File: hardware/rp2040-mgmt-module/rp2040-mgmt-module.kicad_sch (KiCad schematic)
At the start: 38 parts, among them J1 Bus_PCI_Express_x1, J2 USB_B_Micro, J3 RJ45_Hanrun_HR911105A_Horizon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, J4 Conn_01x03_Socket, Q1 2N7002KQ-7, SW1 SW_Push, U1 AMS1117-3.3, U2 W25Q32JVSSIQ, U3 RP2040, U4 W5500, Y1 X322512MSB4SI, Y2 X322512MSB4SI

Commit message: feat: initial rp2040 mgmt module layout finished
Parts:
- removed D1: BAT60B, Diode_SMD:D_SOD-323, symbol Diode:BAT60A
- removed Q1: 2N7002KQ-7, Package_TO_SOT_SMD:SOT-23, symbol Transistor_FET:2N7002
- added C1, C6: 1uF, Capacitor_SMD:C_0402_1005Metric, symbol Device:C
- added C10, C12, C13, C14, C17, C3, C5, C7, C8, C9: 100nF, Capacitor_SMD:C_0402_1005Metric, symbol Device:C
- added C11: 4.7uF, Capacitor_SMD:C_0402_1005Metric, symbol Device:C
- added C15: 22nF, Capacitor_SMD:C_0402_1005Metric, symbol Device:C
- added C16, C18: 6.8nF, Capacitor_SMD:C_0402_1005Metric, symbol Device:C
- added C2, C4: 39pF, Capacitor_SMD:C_0402_1005Metric, symbol Device:C
- added C36: 10uF, Capacitor_SMD:C_0402_1005Metric, symbol Device:C
- added D2: RED, LED_SMD:LED_0603_1608Metric, symbol Device:LED
- added D3: GREEN, LED_SMD:LED_0603_1608Metric, symbol Device:LED
- added D4: Neopixel Side Light SK6812, Local Library:LED_Neopixel_Side_Light_SK6812, symbol usb-pd-psu:LED_Neopixel_Side_Light_SK6812
- added J5: ADC, Connector_PinSocket_2.54mm:PinSocket_1x02_P2.54mm_Vertical, symbol Connector:Conn_01x02_Pin
- added J6: UART, Connector_PinHeader_2.54mm:PinHeader_1x04_P2.54mm_Vertical, symbol Connector:Conn_01x04_Pin
- added J7: UART, Connector_PinHeader_2.54mm:PinHeader_1x06_P2.54mm_Vertical, symbol Connector:Conn_01x06_Pin
- added R1, R3, R5: 4.7K, Resistor_SMD:R_0402_1005Metric, symbol Device:R
- added R10, R12, R13, R14: 49.9R, Resistor_SMD:R_0402_1005Metric, symbol Device:R
- added R11: 12.4K 1%, Resistor_SMD:R_0402_1005Metric, symbol Device:R
- added R15: 10R 1%, Resistor_SMD:R_0402_1005Metric, symbol Device:R
- added R18, R19, R20, R21: 470R, Resistor_SMD:R_0402_1005Metric, symbol Device:R
- added R2, R22: 1K, Resistor_SMD:R_0402_1005Metric, symbol Device:R
- added R23: 200R, Resistor_SMD:R_0402_1005Metric, symbol Device:R
- added R24: 1R, Resistor_SMD:R_0402_1005Metric, symbol Device:R
- added R4: 1M, Resistor_SMD:R_0402_1005Metric, symbol Device:R
- added R6, R7, R8, R9: 3.3R, Resistor_SMD:R_0402_1005Metric, symbol Device:R
- added SW2: RESET, Local Library:XKB_TS-1101_SWITCH, symbol Switch:SW_Push
- C19: renamed from C3; footprint Capacitor_SMD:C_0805_2012Metric -> Capacitor_SMD:C_0402_1005Metric; LCSC (none) -> C15525
- C20: renamed from C4; footprint Capacitor_SMD:C_0805_2012Metric -> Capacitor_SMD:C_0402_1005Metric; LCSC (none) -> C15525
- C21: renamed from C5; LCSC (none) -> C1525
- C22: renamed from C6; LCSC (none) -> C1525
- C23: renamed from C7; LCSC (none) -> C1525
- C24: renamed from C8; LCSC (none) -> C52923
- C25: renamed from C9; LCSC (none) -> C1525
- C26: renamed from C10; LCSC (none) -> C52923
- C27: renamed from C11; LCSC (none) -> C1525
- C30: renamed from C12; LCSC (none) -> C1525
- C31: renamed from C13; LCSC (none) -> C1525
- C32: renamed from C14; LCSC (none) -> C1525
- C33: renamed from C15; LCSC (none) -> C1525
- C34: renamed from C16; footprint Capacitor_SMD:C_0805_2012Metric -> Capacitor_SMD:C_0402_1005Metric; LCSC (none) -> C15525
- C35: renamed from C17; LCSC (none) -> C1525
- J1: renamed from J4; value Conn_01x03_Socket -> SWD; symbol Connector:Conn_01x03_Socket -> Connector:Conn_01x03_Pin; now in the parts list
- J2: renamed from J1; now not fitted
- J3: renamed from J2; footprint Connector_USB:USB_Micro-B_Amphenol_10103594-0001LF_Horizontal -> Connector_USB:USB_Micro-B_XKB_U254-051T-4BH83-F1S; JLCPCB_CORRECTION (none) -> 0;-1.1;0; LCSC (none) -> C319160
- J4: renamed from J3; value RJ45_Hanrun_HR911105A_Horizontal -> RJ45_Hanrun_HR913550A_Horizontal; JLCPCB_CORRECTION (none) -> 4.4;4.4;180
- R16: renamed from R1; LCSC (none) -> C11702
- R17: renamed from R2; now not fitted; now left out of the parts list
- R25: renamed from R4; LCSC (none) -> C25100
- R26: renamed from R5; LCSC (none) -> C25100
- R29: renamed from R3; LCSC (none) -> C11702
- SW1: value SW_Push -> BOOT
- U1: renamed from U4; JLCPCB_CORRECTION (none) -> 0;0;-90
- U2: renamed from U1; JLCPCB_CORRECTION (none) -> 0;0;180
- U3: renamed from U2; JLCPCB_CORRECTION (none) -> 0;0;-90
- Y1: renamed from Y2; value X322512MSB4SI -> X322525MRB4SI
- renumbered C1 to C28, C2 to C29, R6 to R27, R7 to R28, U3 to U4, Y1 to Y2
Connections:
- net ENABLE is gone; now on net I2C_A1: U4.36 (GPIO24)
- net GPIO0 is gone; now on net UART_TX: U4.2 (GPIO0)
- net GPIO22 is gone; now on net I2C_A0: U4.34 (GPIO22)
- net GPIO29_ADC3 is gone; now on net OVERLOAD: U4.41 (GPIO29_ADC3)
- net GPIO6 is gone; now on net LED_DIN: U4.8 (GPIO6)
- net +5V: now also D4.2 (VDD)
- net ALERT: now also J2.B11 (~{WAKE})
- net GND: now also J4.8, J4.SH, U1.14 (AGND), U1.16 (AGND), U1.19 (AGND), U1.29 (GND), U1.3 (AGND), U1.48 (AGND), U1.9 (AGND), Y1.2, Y1.4, C1.2, C10.2, C11.2, C12.2, C13.2, C14.2, C15.1, C17.2, C2.2, C3.2, C36.2, C4.2, C5.2, C6.2, C7.2, C8.2, C9.2, D2.1 (K), D3.1 (K), D4.4 (GND), J6.1 (Pin_1), J7.1 (Pin_1), R11.1, R24.1, SW2.1
- net GPIO10: now also J7.5 (Pin_5)
- net GPIO11: now also J7.6 (Pin_6)
- net GPIO16: now also U1.34 (MISO)
- net GPIO17: now also U1.32 (~{SCS}), R5.2
- net GPIO18: now also U1.33 (SCLK)
- net GPIO19: now also U1.35 (MOSI)
- net GPIO20: now also U1.37 (~{RST}), R1.1
- net GPIO21: now also U1.36 (~{INT}), R3.2
- net GPIO25: now also R21.1
- net GPIO27_ADC1: now also J5.1 (Pin_1)
- net GPIO8: now also J7.3 (Pin_3)
- net GPIO9: now also J7.4 (Pin_4)
- net I2C_A2: now also U4.35 (GPIO23)
- net LED_DIN: now also D4.1 (DIN); no longer U4.3 (GPIO1)
- net OVERLOAD: no longer U4.35 (GPIO23)
- net RUN: now also R22.2
- net at U1.1 (TXN): now also R6.1
- net at U1.10 (EXRES1): now also R11.2
- net +3.3VA: now reaches U1.11 (AVDD), U1.15 (AVDD), U1.17 (AVDD), U1.21 (AVDD), U1.4 (AVDD), U1.8 (AVDD)
- net +3.3VA: now also FB1.2, C10.1, C12.1, C14.1, C17.1, C6.1, C7.1, C8.1, R10.1, R12.1, R15.1
- net at U1.2 (TXP): now also R7.2
- net at U1.20 (TOCAP): now also C11.1
- net at U1.22 (1V2O): now also C9.1
- net LINK_LED: now reaches U1.25 (LINKLED)
- net LINK_LED: now also R20.2
- net ACT_LED: now reaches U1.27 (ACTLED)
- net ACT_LED: now also R19.2
- net +3.3V: now reaches U1.28 (VDD)
- net +3.3V: now also C20.1, C21.1, C25.1, C26.1, C27.1, C30.1, C31.1, C32.1, C33.1, C34.1, C35.1, FB1.1, J2.B10 (3.3Vaux), J4.12, J4.9, R17.1, U1.43 (PMODE2), U1.44 (PMODE1), U1.45 (PMODE0), U2.2 (VO), U3.8 (VCC), U4.1 (IOVDD), U4.10 (IOVDD), U4.22 (IOVDD), U4.33 (IOVDD), U4.42 (IOVDD), U4.44 (VREG_IN), U4.48 (USB_VDD), U4.49 (IOVDD), C1.1, C3.1, C36.1, C5.1, J6.2 (Pin_2), J7.2 (Pin_2), R1.2, R18.1, R23.1, R3.1, R5.1
- net at U1.30 (XI/CLKIN): now also Y1.1, C2.1, R4.1
- net at U1.31 (XO): now also R2.1, R4.2
- net at U1.5 (RXN): now also R9.1
- net at U1.6 (RXP): now also R8.2
- net at Y1.3: now also C4.1, R2.2
- net TX_D+: now reaches J4.1 (TD+)
- net TX_D+: now also R12.2, R7.1
- net at J4.10: now also R20.1
- net at J4.11: now also R19.1
- net TX_D-: now reaches J4.2 (TD-)
- net TX_D-: now also R10.2, R6.2
- net RX_D+: now reaches J4.3 (RD+)
- net RX_D+: now also C16.2
- net at J4.4 (TCT): now also C15.2, R15.2
- net at J4.5 (RCT): now also C13.1, R13.1, R14.1
- net RX_D-: now reaches J4.6 (RD-)
- net RX_D-: now also C18.2
- net UART_TX: now reaches J2.A13 (REFCLK+)
- net UART_TX: now also J6.3 (Pin_3)
- net UART_RX: now reaches J2.A14 (REFCLK-)
- net UART_RX: now also U4.3 (GPIO1), J6.4 (Pin_4)
- removed net +3V3: C20.1, C21.1, C25.1, C26.1, C27.1, C30.1, C31.1, C32.1, C33.1, C34.1, C35.1, J2.B10 (3.3Vaux), R17.1, U2.2 (VO), U3.8 (VCC), U4.1 (IOVDD), U4.10 (IOVDD), U4.22 (IOVDD), U4.33 (IOVDD), U4.42 (IOVDD), U4.43 (ADC_AVDD), U4.44 (VREG_IN), U4.48 (USB_VDD), U4.49 (IOVDD)
- net IMON renamed GPIO28_ADC2
- net GPIO28_ADC2: now also J5.2 (Pin_2)
- net ~{USB_BOOT}: no longer names the net of R16.2, SW1.2
- new net: R22.1, SW2.2
- new net: D2.2 (A), R18.2
- new net: C16.1, R14.2, R8.1
- new net: C18.1, R13.2, R9.2
- new net: D3.2 (A), R21.2
- new net ADC_AVDD: R23.2, R24.2, U4.43 (ADC_AVDD)
- no-connect marks 12 -> 17
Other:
- note added: "RP2040 Crystal"
- note removed: "Crystal"
- moved on the sheet: C19, C20, C21, C22, C23, C24, C25, C26, C27, C28, C29, C30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

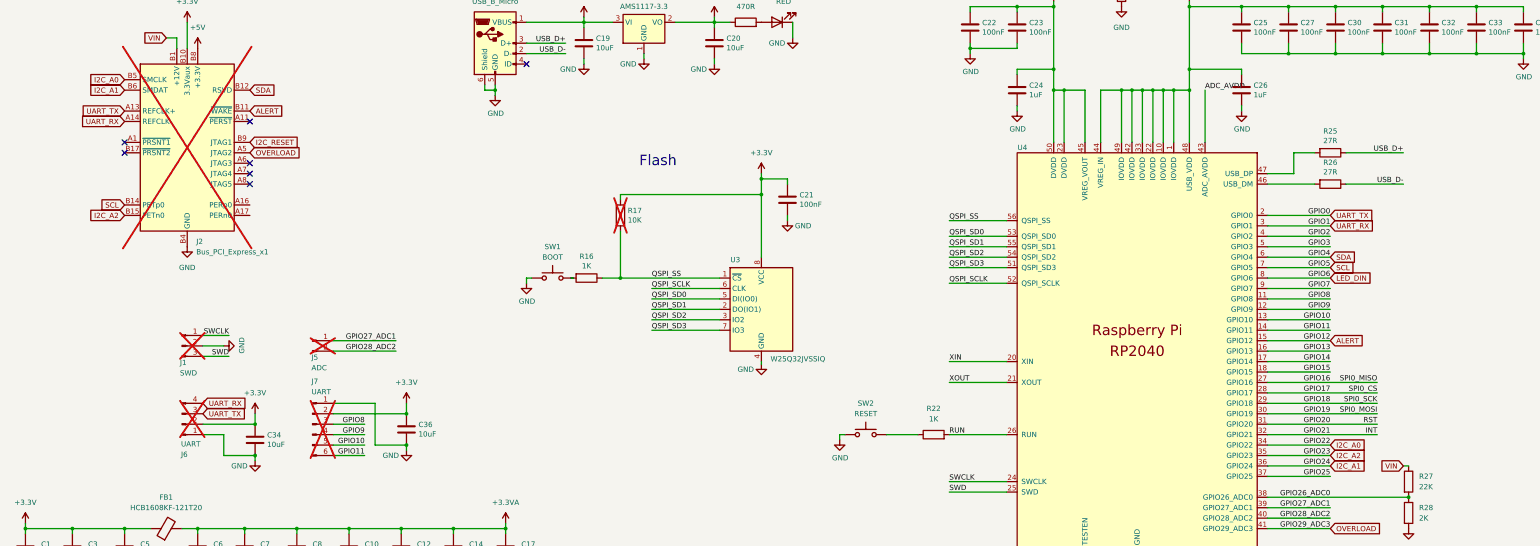
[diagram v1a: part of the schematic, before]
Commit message: feat: add swd circuits for firmware updates
feat: add switch to access onboard rp2040 through charge plug
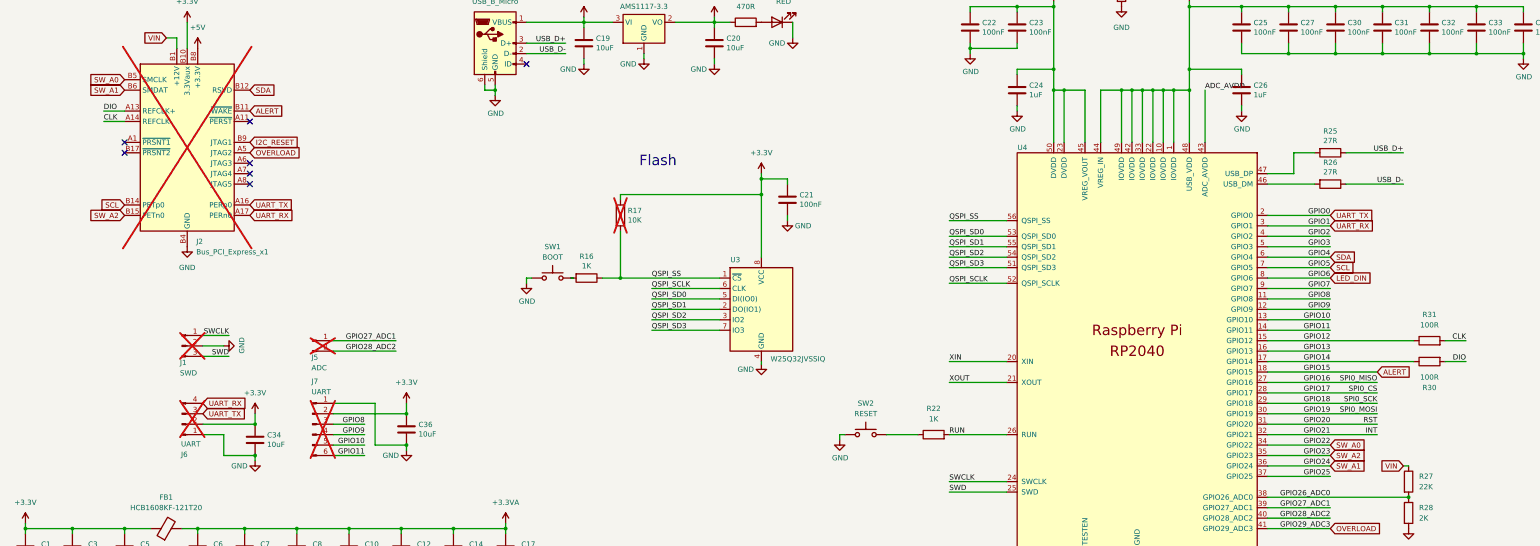
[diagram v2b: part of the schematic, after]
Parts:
- added R30, R31: 100R, Resistor_SMD:R_0402_1005Metric, symbol Device:R
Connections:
- net GPIO15 is gone; now on net ALERT: U4.18 (GPIO15)
- net ALERT: no longer U4.15 (GPIO12)
- net GPIO14: now also R30.1
- net UART_RX: now also J2.A17 (PERn0); no longer J2.A14 (REFCLK-)
- net UART_TX: now also J2.A16 (PERp0); no longer J2.A13 (REFCLK+)
- net I2C_A0 renamed SW_A0
- net I2C_A1 renamed SW_A1
- net I2C_A2 renamed SW_A2
- new net CLK: J2.A14 (REFCLK-), R31.2
- new net DIO: J2.A13 (REFCLK+), R30.2
- new net GPIO12: R31.1, U4.15 (GPIO12)

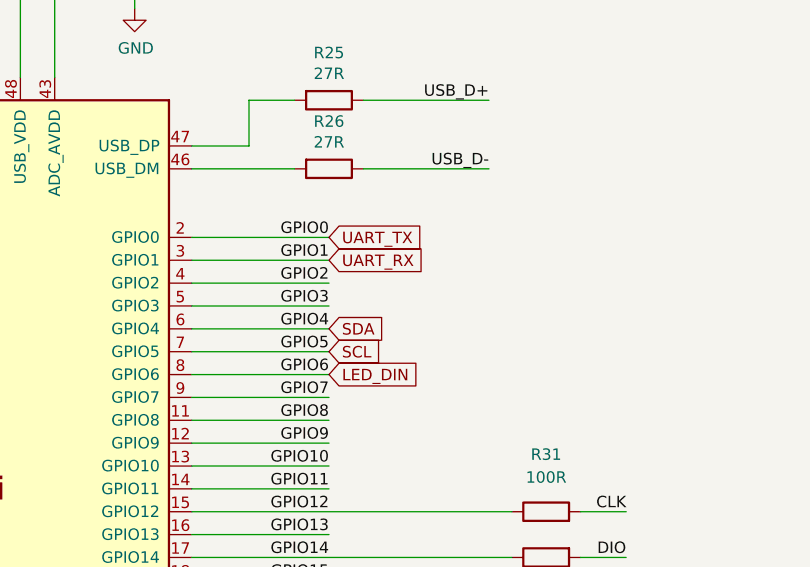
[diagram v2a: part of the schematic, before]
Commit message: fix: can't forget the pull-ups
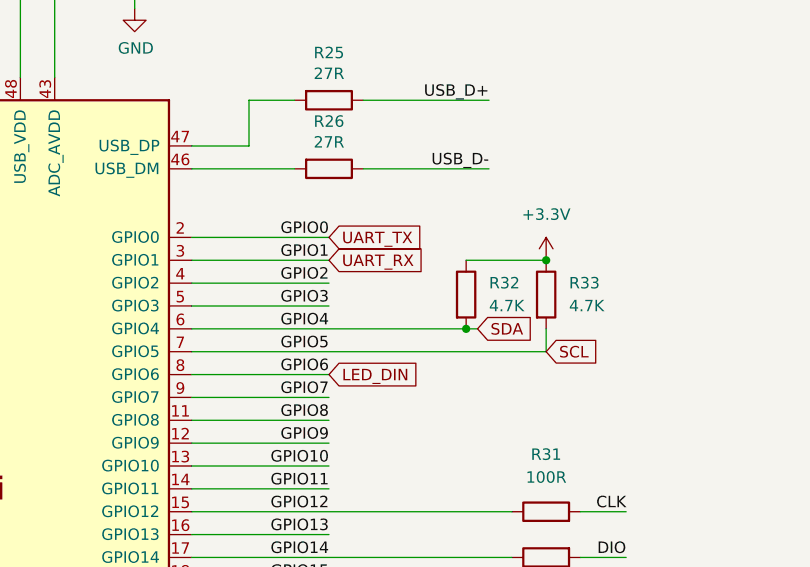
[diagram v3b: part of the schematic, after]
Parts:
- added R32, R33: 4.7K, Resistor_SMD:R_0402_1005Metric, symbol Device:R
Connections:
- net +3.3V: now also R32.1, R33.1
- net SCL: now also R33.2
- net SDA: now also R32.2

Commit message: fix: fix incorrect part numbers
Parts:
- C16, C18: LCSC C1631 -> C1542
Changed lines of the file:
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@@
 			)
 		)
-		(property "LCSC" "C1631"
+		(property "LCSC" "C1542"
 			(at 129.54 215.9 0)
 			(effects
@@
 			)
 		)
-		(property "LCSC" "C1631"
+		(property "LCSC" "C1542"
 			(at 140.97 222.25 0)
 			(effects
